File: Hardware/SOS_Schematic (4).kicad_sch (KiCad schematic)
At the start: 42 parts, among them J1 USB_B_Mini, J2 Conn_02x10_Odd_Even, J3 Conn_01x02, SW1 SW_SPDT, U1 BU33SD5WG-TR, U2 STM32L476RGTx, U3 HTRC11001T, Y1 13,56MHz, Y2 8MHz

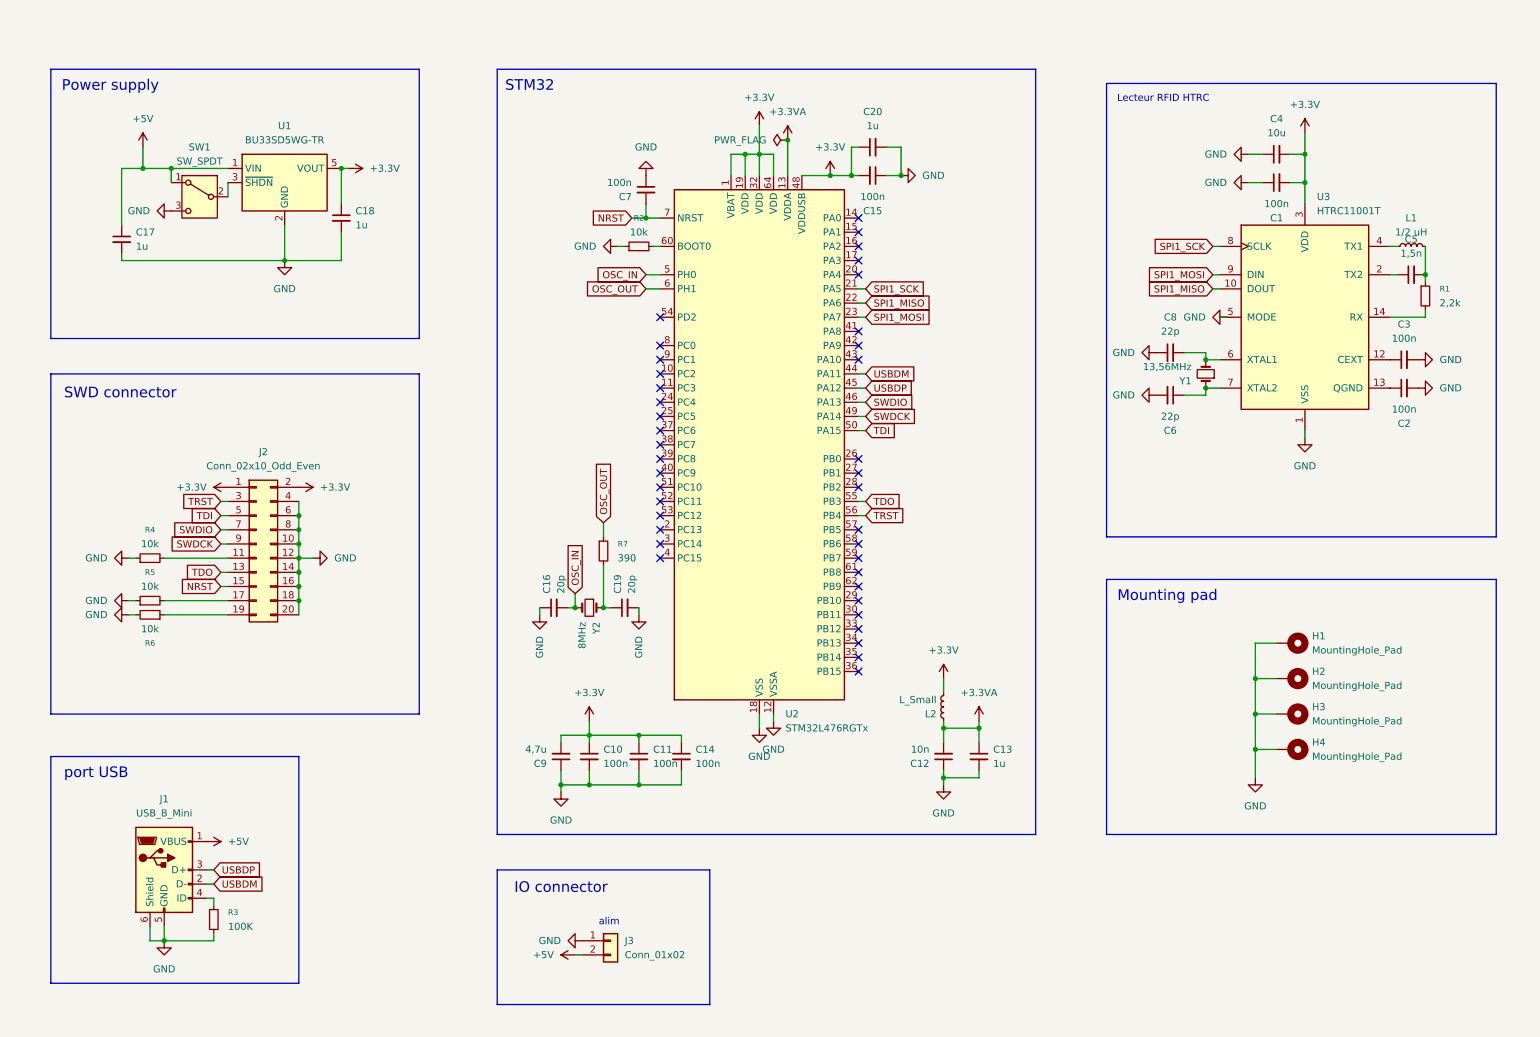
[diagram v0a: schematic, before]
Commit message: update schematic, create stm32cubeide project with pinout
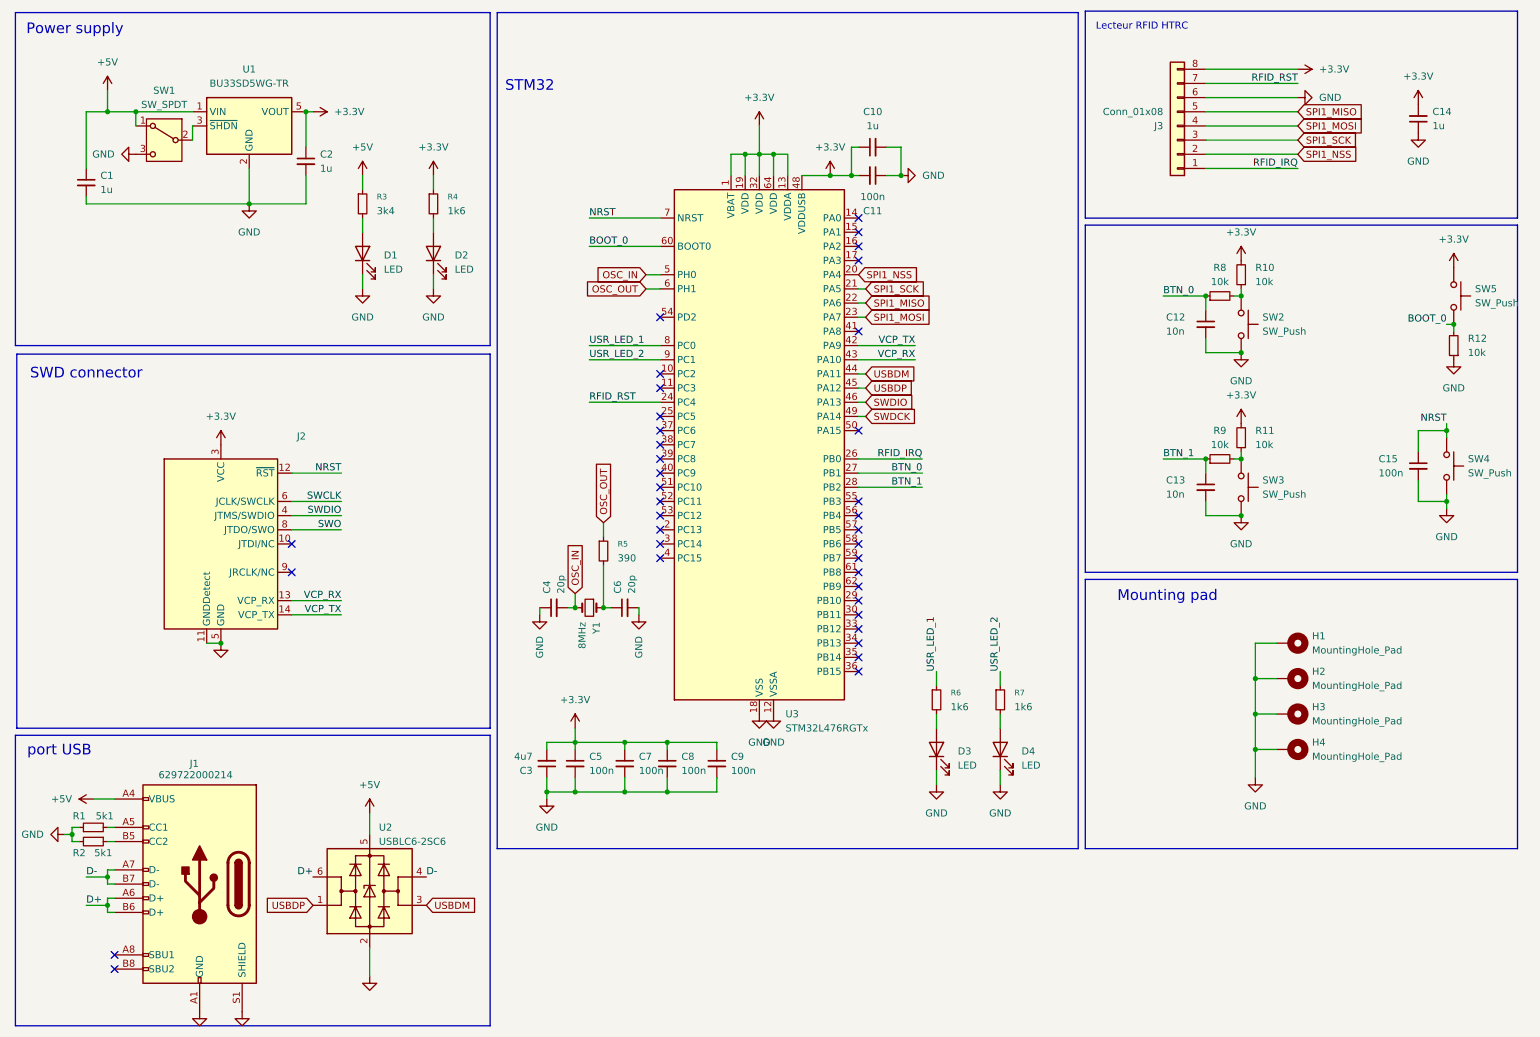
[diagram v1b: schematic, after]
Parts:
- removed C1, C2, C3, C7: 100n, Capacitor_SMD:C_0603_1608Metric_Pad1.08x0.95mm_HandSolder, symbol Device:C_Small
- removed C4: 10u, Capacitor_SMD:C_0603_1608Metric_Pad1.08x0.95mm_HandSolder, symbol Device:C_Small
- removed C5: 1,5n, Capacitor_SMD:C_0603_1608Metric_Pad1.08x0.95mm_HandSolder, symbol Device:C_Small
- removed C6, C8: 22p, Capacitor_SMD:C_0603_1608Metric_Pad1.08x0.95mm_HandSolder, symbol Device:C_Small
- removed J1: USB_B_Mini, Connector_USB:USB_Mini-B_Tensility_54-00023_Vertical, symbol Connector:USB_B_Mini
- removed J2: Conn_02x10_Odd_Even, Connector_PinHeader_1.27mm:PinHeader_2x10_P1.27mm_Vertical, symbol Connector_Generic:Conn_02x10_Odd_Even
- removed J3: Conn_01x02, Connector_JST:JST_XH_B2B-XH-A_1x02_P2.50mm_Vertical, symbol Connector_Generic:Conn_01x02
- removed L1: 1/2 uH, Inductor_SMD:L_0805_2012Metric_Pad1.05x1.20mm_HandSolder, symbol Device:L_Small
- removed L2: L_Small, Inductor_SMD:L_0805_2012Metric_Pad1.05x1.20mm_HandSolder, symbol Device:L_Small
- removed R5: 10k, Resistor_SMD:R_0805_2012Metric_Pad1.20x1.40mm_HandSolder, symbol Device:R_Small
- removed U3: HTRC11001T, Package_SO:SOIC-14_3.9x8.7mm_P1.27mm, symbol RF_RFID:HTRC11001T
- removed Y1: 13,56MHz, Crystal:Crystal_DS10_D1.0mm_L4.3mm_Vertical, symbol Device:Crystal_Small
- added C14: 1u, Capacitor_SMD:C_0603_1608Metric, symbol Device:C_Small
- added C15: 100n, Capacitor_SMD:C_0402_1005Metric, symbol Device:C_Small
- added C9: 100n, Capacitor_SMD:C_0603_1608Metric, symbol Device:C_Small
- added D1, D2, D3, D4: LED, LED_SMD:LED_0603_1608Metric, symbol Device:LED
- added J1: 629722000214, Connector_USB:USB_C_Receptacle_HRO_TYPE-C-31-M-12, symbol Connector:USB_C_Receptacle_USB2.0_16P
- added J2: ~, Connector_PinHeader_1.27mm:PinHeader_2x07_P1.27mm_Vertical_SMD, symbol Connector:Conn_ST_STDC14
- added J3: Conn_01x08, Connector_PinSocket_2.54mm:PinSocket_1x08_P2.54mm_Vertical, symbol Connector_Generic:Conn_01x08
- added R10, R11, R12, R8, R9: 10k, Resistor_SMD:R_0603_1608Metric, symbol Device:R_Small
- added R7: 1k6, Resistor_SMD:R_0603_1608Metric, symbol Device:R_Small
- added SW2, SW3, SW4, SW5: SW_Push, Maker:KSS221GLFS, symbol Switch:SW_Push
- added U2: USBLC6-2SC6, Package_TO_SOT_SMD:SOT-23-6, symbol Power_Protection:USBLC6-2SC6
- C1: renamed from C17; footprint Capacitor_SMD:C_0603_1608Metric_Pad1.08x0.95mm_HandSolder -> Capacitor_SMD:C_0603_1608Metric
- C10: renamed from C20; footprint Capacitor_SMD:C_0603_1608Metric_Pad1.08x0.95mm_HandSolder -> Capacitor_SMD:C_0603_1608Metric
- C11: renamed from C15; footprint Capacitor_SMD:C_0603_1608Metric_Pad1.08x0.95mm_HandSolder -> Capacitor_SMD:C_0603_1608Metric
- C12: footprint Capacitor_SMD:C_0603_1608Metric_Pad1.08x0.95mm_HandSolder -> Capacitor_SMD:C_0402_1005Metric
- C13: value 1u -> 10n; footprint Capacitor_SMD:C_0603_1608Metric_Pad1.08x0.95mm_HandSolder -> Capacitor_SMD:C_0402_1005Metric
- C2: renamed from C18; footprint Capacitor_SMD:C_0603_1608Metric_Pad1.08x0.95mm_HandSolder -> Capacitor_SMD:C_0603_1608Metric
- C3: renamed from C9; value 4,7u -> 4u7; footprint Capacitor_SMD:C_0603_1608Metric_Pad1.08x0.95mm_HandSolder -> Capacitor_SMD:C_0603_1608Metric
- C4: renamed from C16; footprint Capacitor_SMD:C_0603_1608Metric_Pad1.08x0.95mm_HandSolder -> Capacitor_SMD:C_0402_1005Metric
- C5: renamed from C10; footprint Capacitor_SMD:C_0603_1608Metric_Pad1.08x0.95mm_HandSolder -> Capacitor_SMD:C_0603_1608Metric
- C6: renamed from C19; footprint Capacitor_SMD:C_0603_1608Metric_Pad1.08x0.95mm_HandSolder -> Capacitor_SMD:C_0402_1005Metric
- C7: renamed from C11; footprint Capacitor_SMD:C_0603_1608Metric_Pad1.08x0.95mm_HandSolder -> Capacitor_SMD:C_0603_1608Metric
- C8: renamed from C14; footprint Capacitor_SMD:C_0603_1608Metric_Pad1.08x0.95mm_HandSolder -> Capacitor_SMD:C_0603_1608Metric
- R1: value 2,2k -> 5k1; footprint Resistor_SMD:R_0805_2012Metric_Pad1.20x1.40mm_HandSolder -> Resistor_SMD:R_0603_1608Metric
- R2: value 10k -> 5k1; footprint Resistor_SMD:R_0805_2012Metric_Pad1.20x1.40mm_HandSolder -> Resistor_SMD:R_0603_1608Metric
- R3: value 100K -> 3k4; footprint Resistor_SMD:R_0805_2012Metric_Pad1.20x1.40mm_HandSolder -> Resistor_SMD:R_0603_1608Metric
- R4, R6: value 10k -> 1k6; footprint Resistor_SMD:R_0805_2012Metric_Pad1.20x1.40mm_HandSolder -> Resistor_SMD:R_0603_1608Metric
- R5: renamed from R7; footprint Resistor_SMD:R_0805_2012Metric_Pad1.20x1.40mm_HandSolder -> Resistor_SMD:R_0603_1608Metric
- SW1: footprint Button_Switch_THT:SW_Push_1P2T_Vertical_E-Switch_800UDP8P1A1M6 -> (none)
- Y1: renamed from Y2; footprint Crystal:Crystal_DS10_D1.0mm_L4.3mm_Vertical -> (none)
- renumbered U2 to U3
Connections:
- net +3.3V: now also R4.1, U3.13 (VDDA), C14.2, C9.1, J2.3 (VCC), J3.8 (Pin_8), R10.2, R11.2, SW5.1
- net +5V: now also R3.1, J1.A4 (VBUS), J1.A9 (VBUS), J1.B4 (VBUS), J1.B9 (VBUS), U2.5 (VBUS)
- net GND: now also C12.2, R1.1, R2.2, C14.1, C15.2, C9.2, D1.1 (K), D2.1 (K), D3.1 (K), D4.1 (K), J1.A1 (GND), J1.A12 (GND), J1.B1 (GND), J1.B12 (GND), J1.S1 (SHIELD), J2.11 (GNDDetect), J2.5 (GND), J2.7 (GND), J3.6 (Pin_6), R12.1, SW2.2, SW3.2, SW4.2, U2.2 (GND); no longer C12.1, R2.1, R3.2, R4.1, R6.2
- net NRST: now also C15.1, J2.12 (~{RST}), SW4.1
- net SPI1_MISO: now also J3.5 (Pin_5)
- net SPI1_MOSI: now also J3.4 (Pin_4)
- net SPI1_SCK: now also J3.3 (Pin_3)
- net SWDIO: now also J2.4 (JTMS/SWDIO)
- net USBDM: now also U2.3 (I/O2)
- net USBDP: now also U2.1 (I/O1)
- net at R4.2: now also D2.2 (A)
- net USR_LED_1: now reaches R6.1
- net USR_LED_1: now also U3.8 (PC0)
- net at R1.2: now also J1.A5 (CC1)
- net BOOT_0: now reaches U3.60 (BOOT0)
- net BOOT_0: now also R12.2, SW5.2; no longer R2.2
- net SPI1_NSS: now reaches U3.20 (PA4)
- net SPI1_NSS: now also J3.2 (Pin_2)
- net RFID_RST: now reaches U3.24 (PC4)
- net RFID_RST: now also J3.7 (Pin_7)
- net RFID_IRQ: now reaches U3.26 (PB0)
- net RFID_IRQ: now also J3.1 (Pin_1)
- net BTN_0: now reaches U3.27 (PB1)
- net BTN_0: now also C12.1, R8.1
- net BTN_1: now reaches U3.28 (PB2)
- net BTN_1: now also C13.1, R9.1
- net VCP_TX: now reaches U3.42 (PA9)
- net VCP_TX: now also J2.14 (VCP_TX)
- net VCP_RX: now reaches U3.43 (PA10)
- net VCP_RX: now also J2.13 (VCP_RX)
- net USR_LED_2: now reaches U3.9 (PC1)
- net USR_LED_2: now also R7.1
- removed net +3.3VA: C12.2, C13.1, U3.13 (VDDA)
- net TDI: no longer names the net of U3.50 (PA15)
- net TDO: no longer names the net of U3.55 (PB3)
- net TRST: no longer names the net of U3.56 (PB4)
- new net: D3.2 (A), R6.2
- new net: D1.2 (A), R3.2
- new net: R10.1, R8.2, SW2.1
- new net: R11.1, R9.2, SW3.1
- new net: D4.2 (A), R7.2
- new net: J1.B5 (CC2), R2.1
- new net D+: J1.A6 (D+), J1.B6 (D+), U2.6 (I/O1)
- new net D-: J1.A7 (D-), J1.B7 (D-), U2.4 (I/O2)
- new net SWCLK: J2.6 (JCLK/SWCLK)
- new net SWO: J2.8 (JTDO/SWO)
- no-connect marks 39 -> 37
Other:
- note removed: "IO connector"
- note removed: "alim"
- moved on the sheet: C1, C2, C3, C5, C7, C8, SW1, U1
